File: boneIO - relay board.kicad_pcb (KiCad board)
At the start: 2 copper layers, 197 x 102 mm, 76 parts, among them J1 Screw_Terminal_01x04, J10 Screw_Terminal_01x04, J11 Screw_Terminal_01x04, J12 Screw_Terminal_01x04, J13 Screw_Terminal_01x04, J2 Screw_Terminal_01x04, J3 Conn_02x04_Odd_Even, J4 Screw_Terminal_01x04, J5 Screw_Terminal_01x04, J6 Screw_Terminal_01x04, J7 Screw_Terminal_01x04, J8 Screw_Terminal_01x04, J9 Screw_Terminal_01x04, K1 RM85-2011-35-1024, K10 RM85-2011-35-1024, K11 RM85-2011-35-1024, K12 RM85-2011-35-1024, K13 RM85-2011-35-1024, K14 RM85-2011-35-1024, K15 RM85-2011-35-1024, K16 RM85-2011-35-1024, K17 RM85-2011-35-1024, K18 RM85-2011-35-1024, K19 RM85-2011-35-1024, K2 RM85-2011-35-1024, K20 RM85-2011-35-1024, K21 RM85-2011-35-1024, K22 RM85-2011-35-1024, K23 RM85-2011-35-1024, K24 RM85-2011-35-1024, K3 RM85-2011-35-1024, K4 RM85-2011-35-1024, K5 RM85-2011-35-1024, K6 RM85-2011-35-1024, K7 RM85-2011-35-1024, K8 RM85-2011-35-1024, K9 RM85-2011-35-1024, U1 MCP9808-E_SO8, U2 MCP9808-E_MS, U3 ULN2803A, U4 ULN2803A, U5 ULN2803A, U6 MCP23017_SS, U7 MCP23017_SS

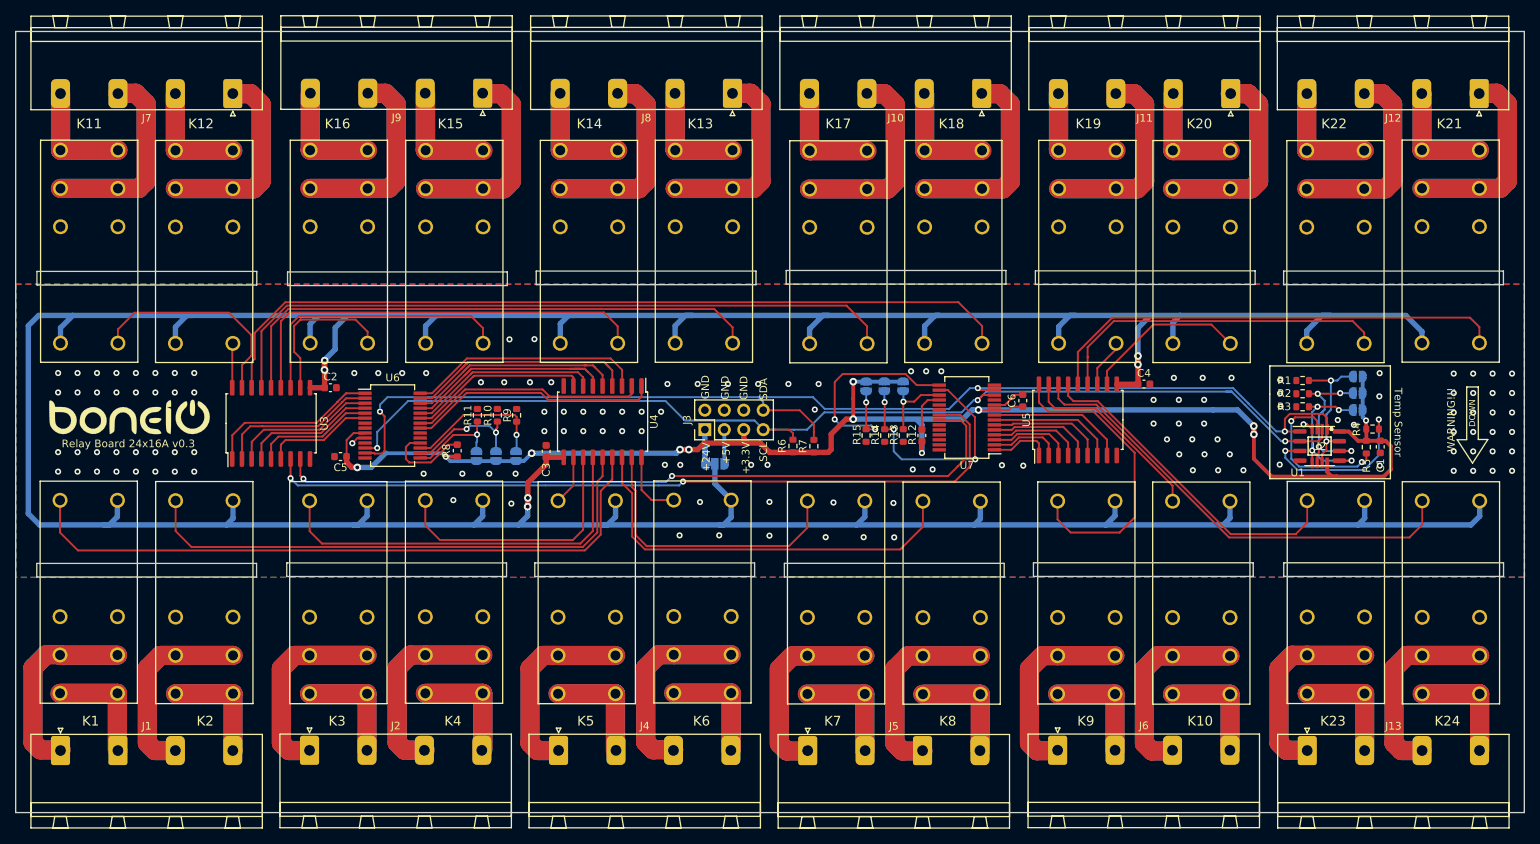
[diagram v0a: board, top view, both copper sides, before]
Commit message: relay board 24x16A v0.4
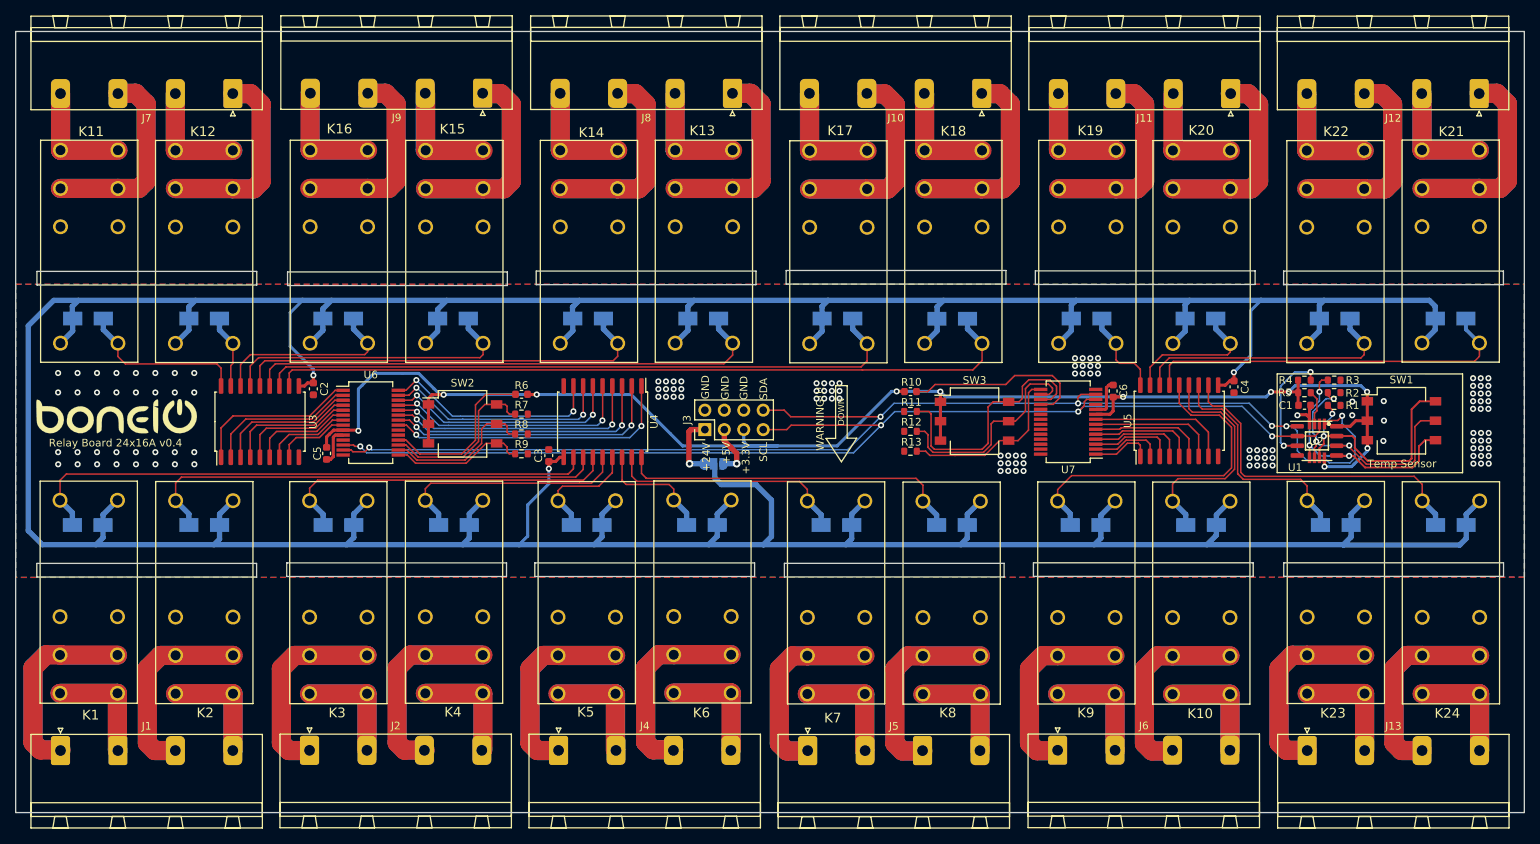
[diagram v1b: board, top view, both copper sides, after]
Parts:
- removed A0 (x2), A1 (x2), A2 (x2), JP2, JP3: NO_Small, Jumper:SolderJumper-2_P1.3mm_Open_RoundedPad1.0x1.5mm
- removed JP4: SolderJumper_3_Bridged12, Jumper:SolderJumper-3_P1.3mm_Bridged12_RoundedPad1.0x1.5mm
- removed the R6 at (389.6, 317.8)
- removed the R7 at (392.4, 317.9)
- added D1: 4007, Diode_SMD:D_SMA, B.Cu at (297.5, 328.2)
- added D10: 4007, Diode_SMD:D_SMA, B.Cu at (442.9, 328.2)
- added D11: 4007, Diode_SMD:D_SMA, B.Cu at (297.6, 301.2)
- added D12: 4007, Diode_SMD:D_SMA, B.Cu at (312.8, 301.2)
- added D13: 4007, Diode_SMD:D_SMA, B.Cu at (377.9, 301.2)
- added D14: 4007, Diode_SMD:D_SMA, B.Cu at (362.9, 301.2)
- added D15: 4007, Diode_SMD:D_SMA, B.Cu at (345.2, 301.2)
- added D16: 4007, Diode_SMD:D_SMA, B.Cu at (330.2, 301.2)
- added D17: 4007, Diode_SMD:D_SMA, B.Cu at (395.4, 301.2)
- added D18: 4007, Diode_SMD:D_SMA, B.Cu at (410.4, 301.2)
- added D19: 4007, Diode_SMD:D_SMA, B.Cu at (428.0, 301.2)
- added D2: 4007, Diode_SMD:D_SMA, B.Cu at (312.8, 328.2)
- added D20: 4007, Diode_SMD:D_SMA, B.Cu at (442.9, 301.2)
- added D21: 4007, Diode_SMD:D_SMA, B.Cu at (475.5, 301.2)
- added D22: 4007, Diode_SMD:D_SMA, B.Cu at (460.4, 301.2)
- added D23: 4007, Diode_SMD:D_SMA, B.Cu at (460.5, 328.2)
- added D24: 4007, Diode_SMD:D_SMA, B.Cu at (475.6, 328.2)
- added D3: 4007, Diode_SMD:D_SMA, B.Cu at (330.3, 328.2)
- added D4: 4007, Diode_SMD:D_SMA, B.Cu at (345.4, 328.2)
- added D5: 4007, Diode_SMD:D_SMA, B.Cu at (362.7, 328.2)
- added D6: 4007, Diode_SMD:D_SMA, B.Cu at (377.8, 328.2)
- added D7: 4007, Diode_SMD:D_SMA, B.Cu at (395.3, 328.2)
- added D8: 4007, Diode_SMD:D_SMA, B.Cu at (410.4, 328.2)
- added D9: 4007, Diode_SMD:D_SMA, B.Cu at (427.9, 328.2)
- added SW1: SW_DIP_x03, Button_Switch_SMD:SW_DIP_SPSTx03_Slide_Omron_A6S-310x_W8.9mm_P2.54mm, F.Cu at (469.1, 314.5)
- added SW2: SW_DIP_x03, Button_Switch_SMD:SW_DIP_SPSTx03_Slide_Omron_A6S-310x_W8.9mm_P2.54mm, F.Cu at (346.5, 314.9)
- added SW3: SW_DIP_x03, Button_Switch_SMD:SW_DIP_SPSTx03_Slide_Omron_A6S-310x_W8.9mm_P2.54mm, F.Cu at (413.4, 314.6)
- JP1: value NO_Small -> SolderJumper_3_Bridged12; footprint Jumper:SolderJumper-2_P1.3mm_Open_RoundedPad1.0x1.5mm -> Jumper:SolderJumper-3_P1.3mm_Bridged12_RoundedPad1.0x1.5mm
- moved JP1 84.9 mm to (379.3, 320.2), turned to 0 degrees
- moved U7 13.3 mm to (425.6, 314.7)
- moved U5 13.2 mm to (440.1, 314.5)
- moved C6 11.9 mm to (431.4, 310.7)
- moved C4 11.8 mm to (447.2, 310.1), turned to -90 degrees
- moved C1 11.3 mm to (456.4, 312.5), turned to 0 degrees
- moved R6 11.2 mm to (354.2, 311.1), turned to 180 degrees
- moved R4 11.0 mm to (456.4, 309.2)
- moved R5 10.8 mm to (456.4, 310.9), turned to 0 degrees
- moved R9 7.65 mm to (354.2, 318.9), turned to 0 degrees
- moved R13 6.15 mm to (405.0, 318.5), turned to 180 degrees
- moved R10 5.92 mm to (405.0, 310.7), turned to 0 degrees
- moved R3 5.39 mm to (460.3, 309.2), turned to 0 degrees
- moved R1 5.25 mm to (460.3, 312.5), turned to 0 degrees
- moved R2 4.12 mm to (460.3, 310.9), turned to 0 degrees
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- renumbered R12 to R10, R13 to R11, R14 to R12, R15 to R13, R8 to R6, R9 to R7, R10 to R8, R11 to R9
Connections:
- JP1 pad 1: +3V3 -> +24V
- JP1 pad 2: Net-(JP1-Pad2) -> VCC
- K1 pad 12: Net-(K1-Pad12) -> unconnected-(K1-Pad12)
- K1 pad 22: Net-(K1-Pad22) -> unconnected-(K1-Pad22)
- K1 pad A1: RELAY1 -> RELAY13
- K10 pad 12: Net-(K10-Pad12) -> unconnected-(K10-Pad12)
- K10 pad 22: Net-(K10-Pad22) -> unconnected-(K10-Pad22)
- K10 pad A1: RELAY10 -> RELAY22
- K11 pad 12: Net-(K11-Pad12) -> unconnected-(K11-Pad12)
- K11 pad 22: Net-(K11-Pad22) -> unconnected-(K11-Pad22)
- K11 pad A1: RELAY11 -> RELAY1
- K12 pad 12: Net-(K12-Pad12) -> unconnected-(K12-Pad12)
- K12 pad 22: Net-(K12-Pad22) -> unconnected-(K12-Pad22)
- K12 pad A1: RELAY12 -> RELAY2
- K13 pad 12: Net-(K13-Pad12) -> unconnected-(K13-Pad12)
- K13 pad 22: Net-(K13-Pad22) -> unconnected-(K13-Pad22)
- K13 pad A1: RELAY16 -> RELAY6
- K14 pad 12: Net-(K14-Pad12) -> unconnected-(K14-Pad12)
- K14 pad 22: Net-(K14-Pad22) -> unconnected-(K14-Pad22)
- K14 pad A1: RELAY15 -> RELAY5
- K15 pad 12: Net-(K15-Pad12) -> unconnected-(K15-Pad12)
- K15 pad 22: Net-(K15-Pad22) -> unconnected-(K15-Pad22)
- K15 pad A1: RELAY14 -> RELAY4
- K16 pad 12: Net-(K16-Pad12) -> unconnected-(K16-Pad12)
- K16 pad 22: Net-(K16-Pad22) -> unconnected-(K16-Pad22)
- K16 pad A1: RELAY13 -> RELAY3
- K17 pad 12: Net-(K17-Pad12) -> unconnected-(K17-Pad12)
- K17 pad 22: Net-(K17-Pad22) -> unconnected-(K17-Pad22)
- K17 pad A1: RELAY17 -> RELAY7
- K18 pad 12: Net-(K18-Pad12) -> unconnected-(K18-Pad12)
- K18 pad 22: Net-(K18-Pad22) -> unconnected-(K18-Pad22)
- K18 pad A1: RELAY18 -> RELAY8
- K19 pad 12: Net-(K19-Pad12) -> unconnected-(K19-Pad12)
- K19 pad 22: Net-(K19-Pad22) -> unconnected-(K19-Pad22)
- K19 pad A1: RELAY19 -> RELAY9
- K2 pad 12: Net-(K2-Pad12) -> unconnected-(K2-Pad12)
- K2 pad 22: Net-(K2-Pad22) -> unconnected-(K2-Pad22)
- K2 pad A1: RELAY2 -> RELAY14
- K20 pad 12: Net-(K20-Pad12) -> unconnected-(K20-Pad12)
- K20 pad 22: Net-(K20-Pad22) -> unconnected-(K20-Pad22)
- K20 pad A1: RELAY20 -> RELAY10
- K21 pad 12: Net-(K21-Pad12) -> unconnected-(K21-Pad12)
- K21 pad 22: Net-(K21-Pad22) -> unconnected-(K21-Pad22)
- K21 pad A1: RELAY21 -> RELAY12
- K22 pad 12: Net-(K22-Pad12) -> unconnected-(K22-Pad12)
- K22 pad 22: Net-(K22-Pad22) -> unconnected-(K22-Pad22)
- K22 pad A1: RELAY22 -> RELAY11
- K23 pad 12: Net-(K23-Pad12) -> unconnected-(K23-Pad12)
- K23 pad 22: Net-(K23-Pad22) -> unconnected-(K23-Pad22)
- K24 pad 12: Net-(K24-Pad12) -> unconnected-(K24-Pad12)
- K24 pad 22: Net-(K24-Pad22) -> unconnected-(K24-Pad22)
- K3 pad 12: Net-(K3-Pad12) -> unconnected-(K3-Pad12)
- K3 pad 22: Net-(K3-Pad22) -> unconnected-(K3-Pad22)
- K3 pad A1: RELAY3 -> RELAY15
- K4 pad 12: Net-(K4-Pad12) -> unconnected-(K4-Pad12)
- K4 pad 22: Net-(K4-Pad22) -> unconnected-(K4-Pad22)
- K4 pad A1: RELAY4 -> RELAY16
- K5 pad 12: Net-(K5-Pad12) -> unconnected-(K5-Pad12)
- K5 pad 22: Net-(K5-Pad22) -> unconnected-(K5-Pad22)
- K5 pad A1: RELAY5 -> RELAY17
- K6 pad 12: Net-(K6-Pad12) -> unconnected-(K6-Pad12)
- K6 pad 22: Net-(K6-Pad22) -> unconnected-(K6-Pad22)
- K6 pad A1: RELAY6 -> RELAY18
- K7 pad 12: Net-(K7-Pad12) -> unconnected-(K7-Pad12)
- K7 pad 22: Net-(K7-Pad22) -> unconnected-(K7-Pad22)
- K7 pad A1: RELAY7 -> RELAY19
- K8 pad 12: Net-(K8-Pad12) -> unconnected-(K8-Pad12)
- K8 pad 22: Net-(K8-Pad22) -> unconnected-(K8-Pad22)
- K8 pad A1: RELAY8 -> RELAY20
- K9 pad 12: Net-(K9-Pad12) -> unconnected-(K9-Pad12)
- K9 pad 22: Net-(K9-Pad22) -> unconnected-(K9-Pad22)
- K9 pad A1: RELAY9 -> RELAY21
- R1 pad 1: Net-(JP1-Pad2) -> Net-(R1-Pad1)
- U1 pad 7: Net-(JP1-Pad2) -> Net-(R1-Pad1)
- U2 pad 7: Net-(JP1-Pad2) -> Net-(R1-Pad1)
- U3 pad 11: RELAY13 -> RELAY8
- U3 pad 12: RELAY14 -> RELAY7
- U3 pad 13: RELAY15 -> RELAY6
- U3 pad 14: RELAY16 -> RELAY5
- U3 pad 15: RELAY17 -> RELAY4
- U3 pad 16: RELAY18 -> RELAY3
- U3 pad 17: RELAY11 -> RELAY2
- U3 pad 18: RELAY12 -> RELAY1
- U3 pad 7: K21 -> K7
- U3 pad 8: K22 -> K8
- U4 pad 1: K23 -> K9
- U4 pad 11: RELAY5 -> RELAY13
- U4 pad 12: RELAY4 -> RELAY14
- U4 pad 13: RELAY3 -> RELAY15
- U4 pad 14: RELAY2 -> RELAY16
- U4 pad 15: RELAY1 -> RELAY17
- U4 pad 16: RELAY8 -> RELAY18
- U4 pad 17: RELAY7 -> RELAY19
- U4 pad 18: RELAY6 -> RELAY20
- U4 pad 2: K24 -> K10
- U4 pad 3: K16 -> K11
- U4 pad 4: K15 -> K12
- U4 pad 5: K14 -> K13
- U4 pad 6: K13 -> K14
- U4 pad 7: K12 -> K15
- U4 pad 8: K11 -> K16
- U5 pad 1: K10 -> K17
- U5 pad 11: RELAY20 -> RELAY24
- U5 pad 12: RELAY19 -> RELAY23
- U5 pad 15: RELAY23 -> RELAY12
- U5 pad 16: RELAY24 -> RELAY11
- U5 pad 2: K9 -> K18
- U5 pad 3: K8 -> K19
- U5 pad 4: K7 -> K20
- U5 pad 5: K20 -> K21
- U5 pad 6: K19 -> K22
- U5 pad 7: K18 -> K23
- U5 pad 8: K17 -> K24
- U6 pad 11: Net-(U6-Pad11) -> unconnected-(U6-Pad11)
- U6 pad 14: Net-(U6-Pad14) -> unconnected-(U6-Pad14)
- U6 pad 19: Net-(U6-Pad19) -> unconnected-(U6-Pad19)
- U6 pad 20: Net-(U6-Pad20) -> unconnected-(U6-Pad20)
- U6 pad 21: K23 -> K9
- U6 pad 22: K24 -> K10
- U6 pad 7: Net-(U6-Pad7) -> K7
- U6 pad 8: Net-(U6-Pad8) -> K8
- U7 pad 1: K10 -> K17
- U7 pad 11: Net-(U7-Pad11) -> unconnected-(U7-Pad11)
- U7 pad 14: Net-(U7-Pad14) -> unconnected-(U7-Pad14)
- U7 pad 19: Net-(U7-Pad19) -> unconnected-(U7-Pad19)
- U7 pad 2: K9 -> K18
- U7 pad 20: Net-(U7-Pad20) -> unconnected-(U7-Pad20)
- U7 pad 21: K21 -> unconnected-(U7-Pad21)
- U7 pad 22: K22 -> unconnected-(U7-Pad22)
- U7 pad 23: Net-(U7-Pad23) -> unconnected-(U7-Pad23)
- U7 pad 24: Net-(U7-Pad24) -> unconnected-(U7-Pad24)
- U7 pad 25: Net-(U7-Pad25) -> unconnected-(U7-Pad25)
- U7 pad 26: Net-(U7-Pad26) -> unconnected-(U7-Pad26)
- U7 pad 27: Net-(U7-Pad27) -> unconnected-(U7-Pad27)
- U7 pad 28: Net-(U7-Pad28) -> unconnected-(U7-Pad28)
- U7 pad 3: K8 -> K19
- U7 pad 4: K7 -> K20
- U7 pad 5: K20 -> K21
- U7 pad 6: K19 -> K22
- U7 pad 7: K18 -> K23
- U7 pad 8: K17 -> K24
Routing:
- net RELAY18: track 107.5 -> 15.6 mm
- net K21: track 102.6 -> 13.9 mm, vias 2 -> 0
- net K22: track 98.8 -> 15.2 mm, vias 2 -> 0
- net VCC: track 543.3 -> 621.3 mm, vias 6 -> 3
- net RELAY17: track 91.3 -> 15.3 mm
- net RELAY1: track 87.4 -> 22.3 mm
- net RELAY2: track 70.8 -> 9.65 mm
- net RELAY6: track 9.02 -> 68.9 mm
- net RELAY13: track 20.5 -> 75.7 mm
- net RELAY5: track 6.51 -> 55.6 mm
- net RELAY7: track 37.9 -> 85.4 mm
- net RELAY8: track 54.1 -> 99.1 mm
- net RELAY12: track 5.82 -> 49.2 mm
- net RELAY16: track 72.3 -> 31.4 mm
- net Net-(R1-Pad1): track 0.00 -> 31.5 mm, vias 0 -> 2
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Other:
- net class +5V removed
- net class 230v removed
- net class Default removed
- board text added: "Relay Board 24x16A v0.4"
- board text removed: "Relay Board 24x16A v0.3"
